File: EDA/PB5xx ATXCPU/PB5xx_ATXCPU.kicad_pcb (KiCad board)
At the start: 2 copper layers, 25 x 35 mm, 10 parts, among them J1 GND Sense, J2 PWR Battery, J3 GND Main, J4 PWR Main, J5 ATX CPU

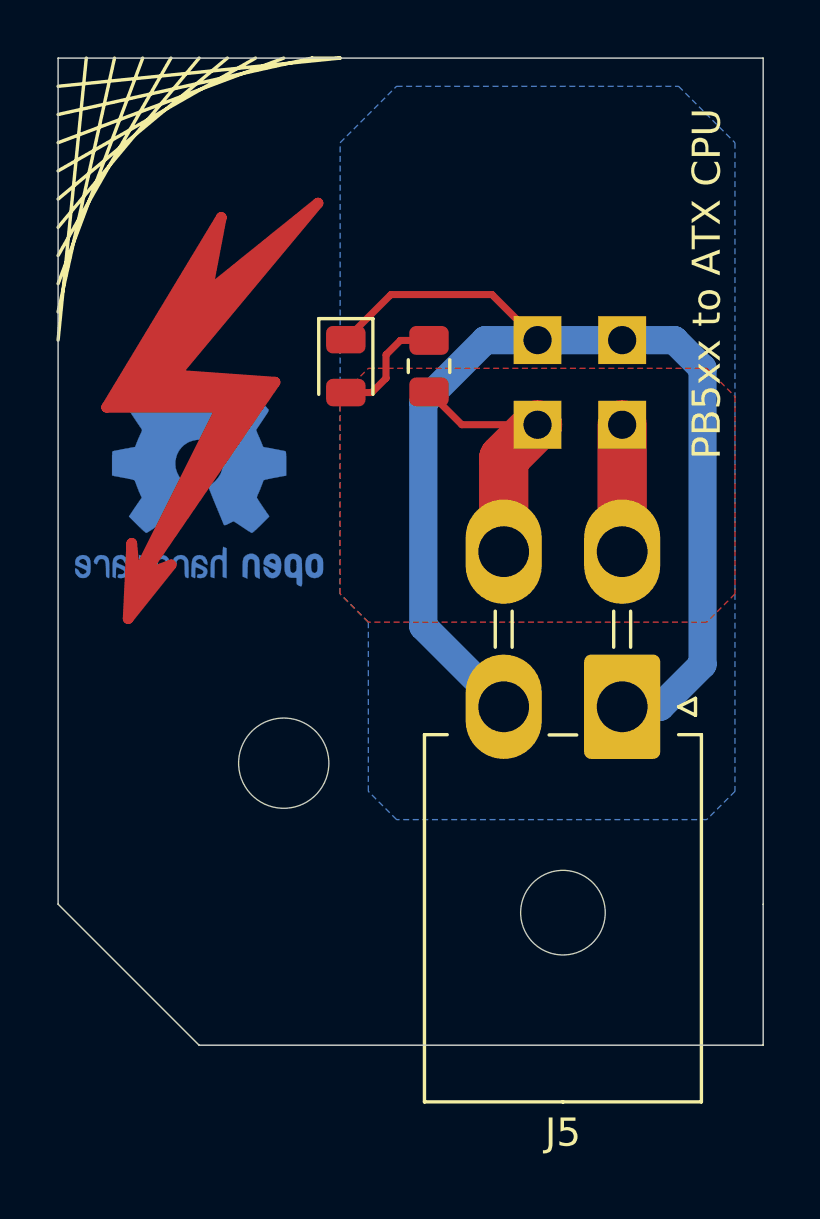
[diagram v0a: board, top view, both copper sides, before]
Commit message: PB5xx ATXCPU v1.3: back to THT, moded to use IDC sockets
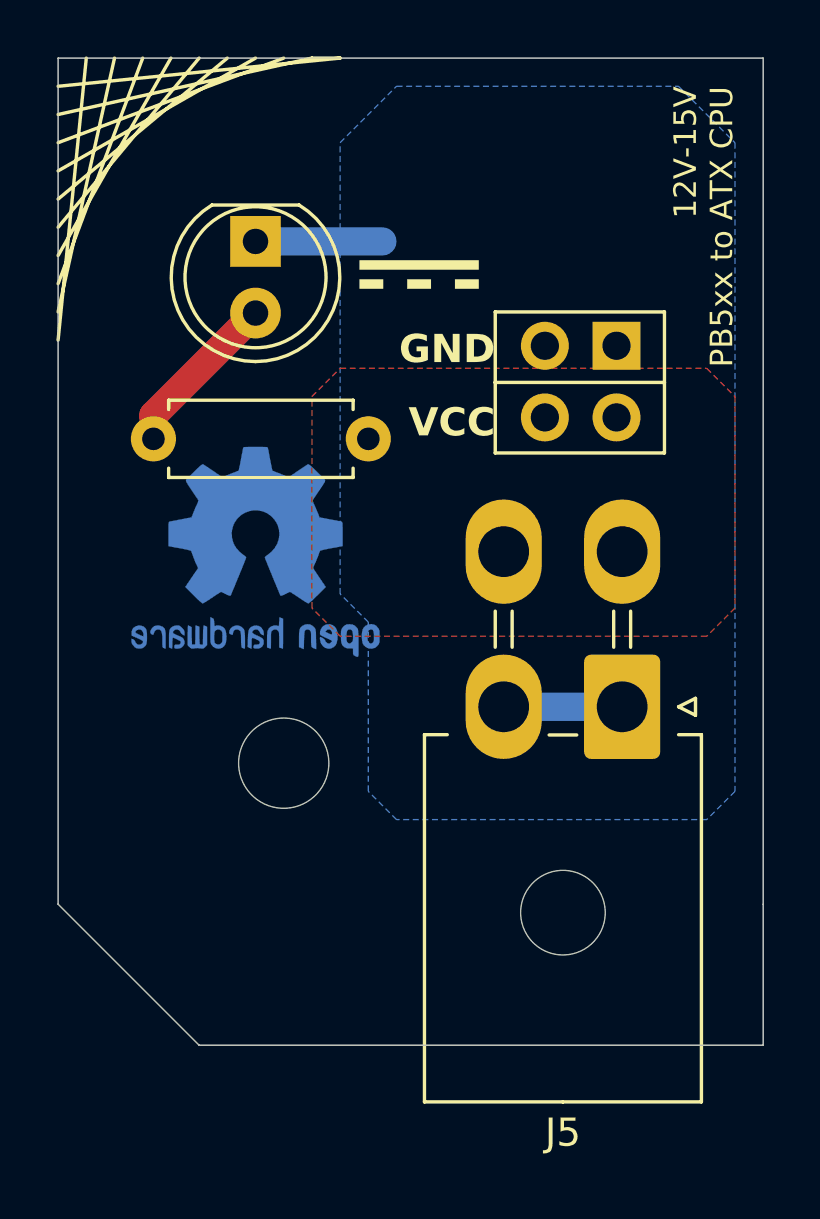
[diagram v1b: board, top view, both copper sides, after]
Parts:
- removed J1: GND Sense, Connector_PinHeader_2.54mm:PinHeader_1x01_P2.54mm_Vertical
- removed J2: PWR Battery, Connector_PinHeader_2.54mm:PinHeader_1x01_P2.54mm_Vertical
- removed J3: GND Main, Connector_PinHeader_2.54mm:PinHeader_1x01_P2.54mm_Vertical
- removed J4: PWR Main, Connector_PinHeader_2.54mm:PinHeader_1x01_P2.54mm_Vertical
- removed the REF** at (64.9, 82.0)
- added DC: LOGO, LOGO, F.Cu at (72.8, 77.8)
- added J6: Conn_02x02_Top_Bottom, Connector_PinSocket_2.54mm:PinSocket_2x02_P2.54mm_Vertical, B.Cu at (79.8, 80.2)
- D1: footprint LED_SMD:LED_0805_2012Metric -> LED_THT:LED_D5.0mm
- R1: value 4700 -> 2200; footprint Resistor_SMD:R_0805_2012Metric -> Resistor_THT:R_Axial_DIN0207_L6.3mm_D2.5mm_P7.62mm_Horizontal
- moved D1 5.46 mm to (67.0, 76.5)
- moved R1 3.36 mm to (71.0, 83.5), turned to 180 degrees
- moved REF** 3.20 mm to (67.0, 87.5)
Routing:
- net GND: track 45.3 -> 8.70 mm
- net +12V: track 13.8 -> 0.28 mm
- net Net-(D1-A): track 4.20 -> 5.96 mm
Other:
- board text added: "12V-15V PB5xx to ATX CPU"
- board text added: "GND"
- board text added: "VCC"
- board text removed: "PB5xx to ATX CPU"

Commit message: PB5xx ATXCPU v1.4: add provisioning for small decoupling capacitor
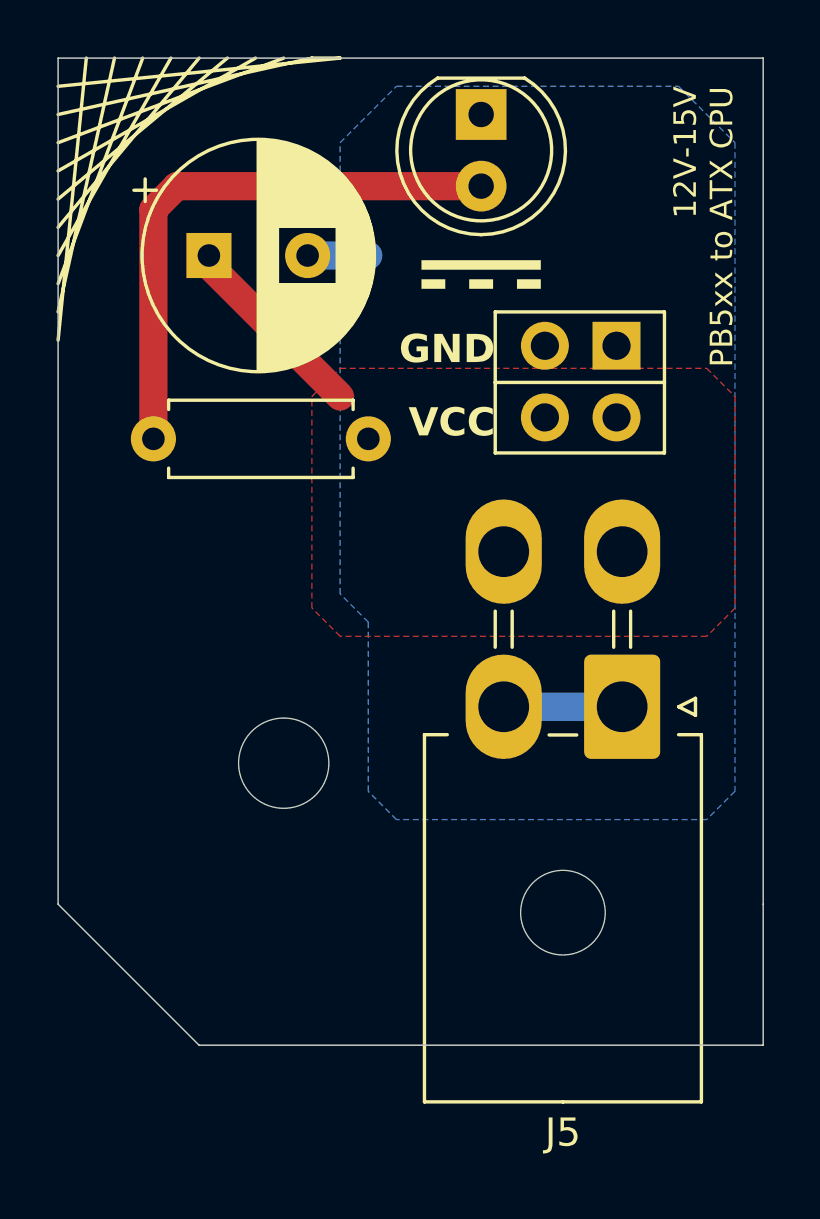
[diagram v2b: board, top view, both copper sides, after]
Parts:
- removed REF**: OSHW-Logo2_9.8x8mm_Copper, Symbol:OSHW-Logo2_9.8x8mm_Copper
- added C1: C_Polarized, Capacitor_THT:CP_Radial_D8.0mm_P3.50mm, F.Cu at (65.3, 77.0)
- R1: value 2200 -> 4300
- moved D1 9.18 mm to (75.0, 72.0)
- moved DC 2.20 mm to (75.0, 77.8)
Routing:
- net Net-(D1-A): track 5.96 -> 20.1 mm
- net +12V: track 0.28 -> 7.21 mm
- net GND: track 8.70 -> 6.35 mm
